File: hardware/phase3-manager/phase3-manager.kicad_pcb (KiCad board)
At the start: 2 copper layers, 100 x 80 mm, 87 parts, among them J1 BACKPLANE, J3 USB-C, J4 UART, J5 PANEL KEYS, J6 ILI9341 LCD MODULE, Q10 2N7002, Q11 AO3401A-class PMOS, Q8 2N7002, Q9 2N7002, SW1 RESET, SW2 BOOT, U10 ESP32-S3-WROOM-1-N8R2, U11 TCAN1042HGV, U12 TPD2E001, U13 TCA9535PWR, U8 LMR36015AQRNXRQ1, U9 NCP1117-3.3

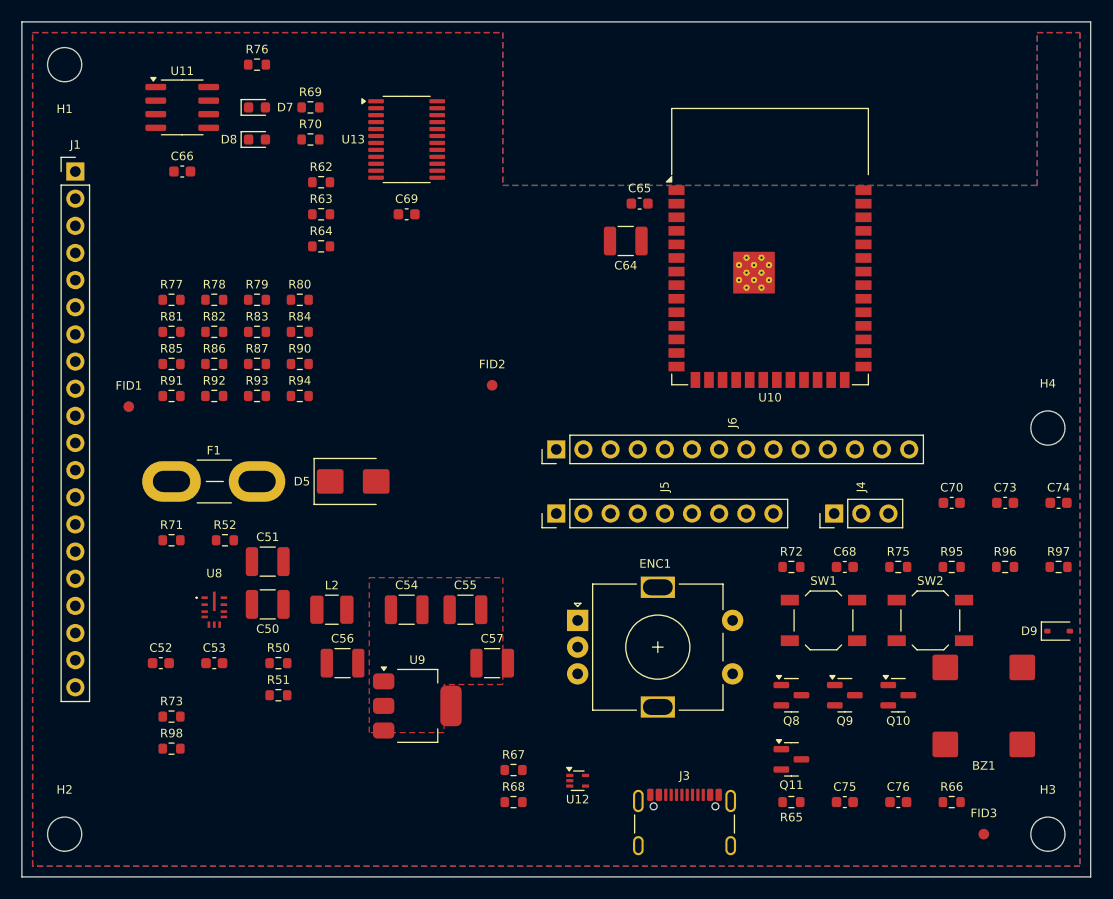
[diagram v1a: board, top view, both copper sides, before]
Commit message: Phase-3 manager: autorouted 173 -> 55 unconnected at ZERO violations
autoroute.py ported from phase-2 + three fixes found on first runs:
- keepout zones (no-net rule areas, the U10 antenna window) now block
  both grid layers — run 1 put 89 items through it. z.Outline().Outline(0)
  is the KiCad-10 accessor; GetOutline does not exist.
- per-pad local clearance honored in the grid (fiducials carry 0.5mm;
  run 2 clipped FID3 twice).
- PARALLEL pre-pass: pad-route A* searches fan out over N forked workers
  (30 on this 32-core box, --jobs=N to override), results merged
  sequentially with re-validation against the live grid + sequential
  fallback per conflict. 291/312 searches parallel; 2.8x CPU. The merge
  stays single-threaded on purpose: parallelism speeds the search, it
  never decides legality.

Remaining 55: 29 power-tie items (PGND/3V3/5V0/VBUS_F — pour spokes,
do last) + 26 signal (USB DP/DN pair, PRESENT3-7, LCD_SCK, KEY4...).
Board state is clean: 0 clearance, 0 keepout, 0 mask violations.
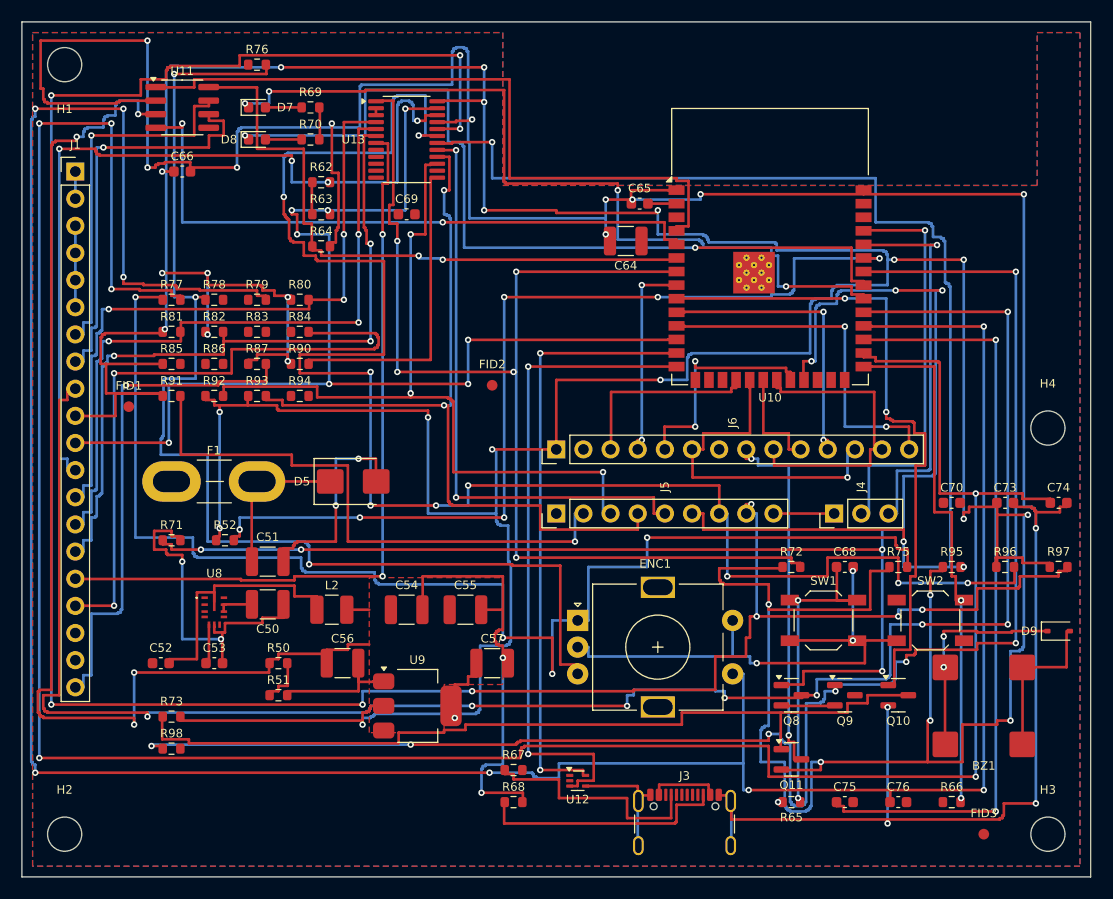
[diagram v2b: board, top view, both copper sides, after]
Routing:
- net 3V3: track 0.00 -> 547.7 mm, vias 0 -> 29
- net PGND: track 0.00 -> 483.2 mm, vias 0 -> 23
- net ENC_SW: track 0.00 -> 260.6 mm, vias 0 -> 8
- net ENC_A: track 0.00 -> 238.7 mm, vias 0 -> 6
- net KEY7: track 0.00 -> 228.4 mm, vias 0 -> 10
- net HW_EN: track 0.00 -> 176.9 mm, vias 0 -> 8
- net KEY6: track 0.00 -> 158.2 mm, vias 0 -> 9
- net BUZZ: track 0.00 -> 154.9 mm, vias 0 -> 7
- net HW_KILL: track 0.00 -> 141.6 mm, vias 0 -> 7
- net 5V0: track 0.00 -> 132.8 mm, vias 0 -> 6
- net ENC_A_RAW: track 0.00 -> 126.8 mm, vias 0 -> 4
- net KEY5: track 0.00 -> 118.6 mm, vias 0 -> 3
- net ENC_B_RAW: track 0.00 -> 111.1 mm, vias 0 -> 3
- net I2C_SDA: track 0.00 -> 109.5 mm, vias 0 -> 8
- net EXP_INT: track 0.00 -> 108.5 mm, vias 0 -> 5
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
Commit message: Phase-3 manager: second autoroute pass on stuck signal nets, 55 -> 54
Multi-pass gains are exhausted: the remaining 25 signal items are local
congestion spots (USB DP/DN at the connector, PRESENT3-7 into J1, the
U8 aux cluster, I2C into the backplane connector) — finish_routes-style
hand waypoints with the analytic validator, or interactive KiCad.
29 power-tie items (PGND/3V3/5V0/VBUS_F spokes) deliberately last.
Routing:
- net LCD_SCK: track 9.23 -> 15.5 mm, vias 0 -> 1
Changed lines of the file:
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@@
+	)
+	(segment
+		(start 89.25 57.875)
+		(end 89.375 57.875)
+		(width 0.25)
+		(layer "F.Cu")
+		(net "LCD_SCK")
 	)
 	(segment
@@
 		(net "LCD_SCK")
 	)
+	(via
+		(at 89.25 57.875)
+		(size 0.6)
+		(drill 0.3)
+		(layers "F.Cu" "B.Cu")
+		(net "LCD_SCK")
+	)
+	(segment
+		(start 86 60)
+		(end 85.24 60)
+		(width 0.25)
+		(layer "B.Cu")
+		(net "LCD_SCK")
+	)
+	(segment
+		(start 86 60)
+		(end 86.375 60)
+		(width 0.25)
+		(layer "B.Cu")
+		(net "LCD_SCK")
+	)
+	(segment
+		(start 86.375 60)
+		(end 86.375 58.5)
+		(width 0.25)
+		(layer "B.Cu")
+		(net "LCD_SCK")
+	)
+	(segment
+		(start 86.375 58.5)
+		(end 89.25 58.5)
+		(width 0.25)
+		(layer "B.Cu")
+		(net "LCD_SCK")
+	)
+	(segment
+		(start 89.25 58.5)
+		(end 89.25 57.875)
+		(width 0.25)
+		(layer "B.Cu")
+		(net "LCD_SCK")
+	)
